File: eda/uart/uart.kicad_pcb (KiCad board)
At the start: 2 copper layers, 20 parts, among them J1 Bus expansion, U1 74HCT193, U2 74HCT165, U3 74HCT165, X1 1.8xx

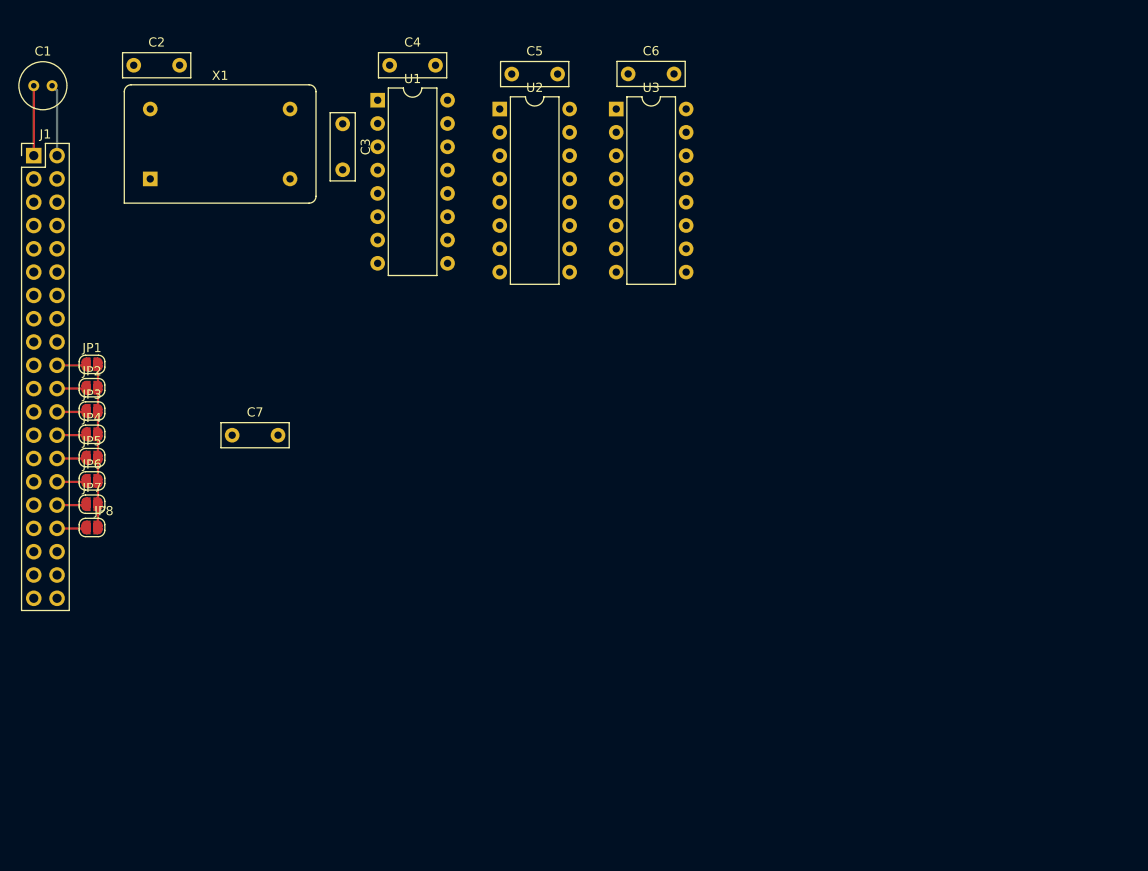
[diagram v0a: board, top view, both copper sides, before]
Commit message: More work on UART
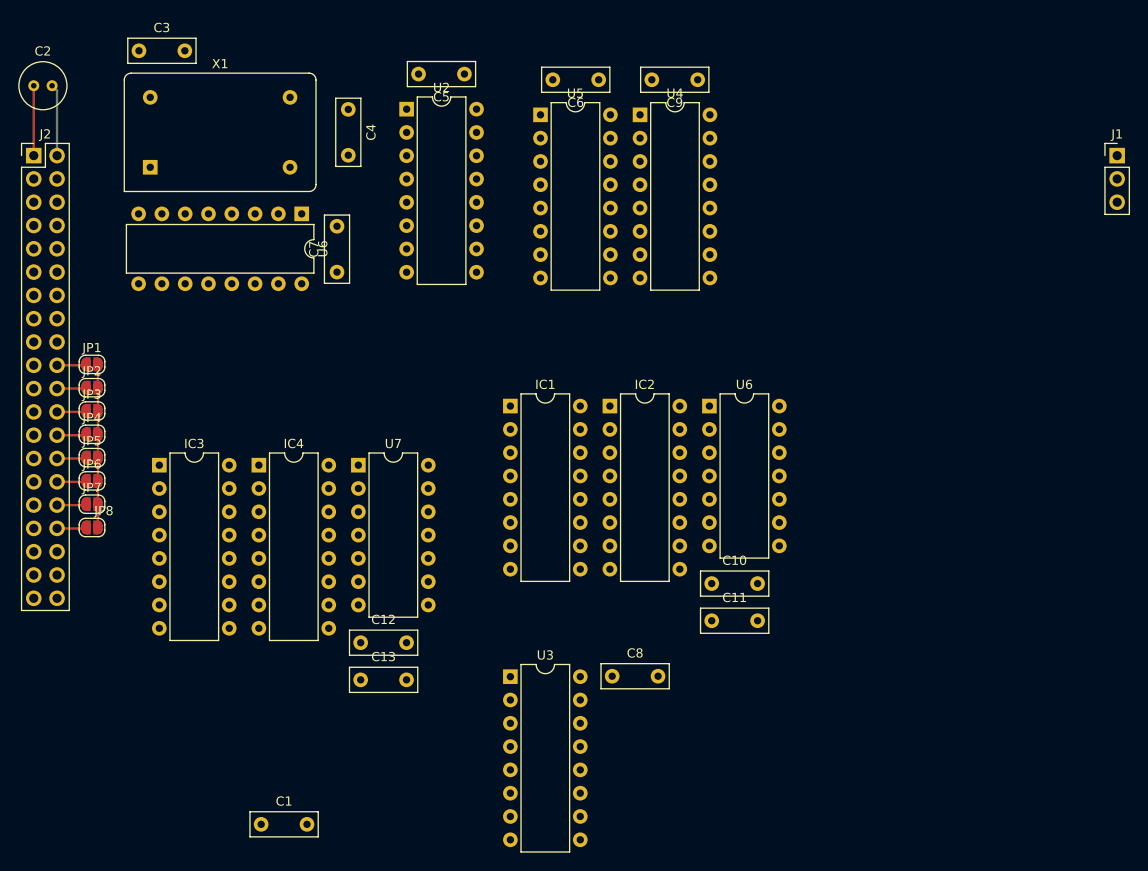
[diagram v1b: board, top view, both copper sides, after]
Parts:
- removed the C2 at (41.4, 81.6)
- removed U1: 74HCT193, Package_DIP:DIP-16_W7.62mm
- added C1: 0.1uf, Capacitor_THT:C_Rect_L7.2mm_W2.5mm_P5.00mm_FKS2_FKP2_MKS2_MKP2, F.Cu at (55.3, 164.3)
- added C10: 0.1uf, Capacitor_THT:C_Rect_L7.2mm_W2.5mm_P5.00mm_FKS2_FKP2_MKS2_MKP2, F.Cu at (104.4, 138.1)
- added C11: 0.1uf, Capacitor_THT:C_Rect_L7.2mm_W2.5mm_P5.00mm_FKS2_FKP2_MKS2_MKP2, F.Cu at (104.4, 142.1)
- added C12: 0.1uf, Capacitor_THT:C_Rect_L7.2mm_W2.5mm_P5.00mm_FKS2_FKP2_MKS2_MKP2, F.Cu at (66.1, 144.5)
- added C13: 0.1uf, Capacitor_THT:C_Rect_L7.2mm_W2.5mm_P5.00mm_FKS2_FKP2_MKS2_MKP2, F.Cu at (66.1, 148.6)
- added C8: 0.1uf, Capacitor_THT:C_Rect_L7.2mm_W2.5mm_P5.00mm_FKS2_FKP2_MKS2_MKP2, F.Cu at (93.5, 148.2)
- added C9: 0.1uf, Capacitor_THT:C_Rect_L7.2mm_W2.5mm_P5.00mm_FKS2_FKP2_MKS2_MKP2, F.Cu at (102.9, 83.2)
- added IC1: CD74HCT40105E, Package_DIP:DIP-16_W7.62mm, F.Cu at (82.4, 118.7)
- added IC2: CD74HCT40105E, Package_DIP:DIP-16_W7.62mm, F.Cu at (93.3, 118.7)
- added IC3: CD74HCT40105E, Package_DIP:DIP-16_W7.62mm, F.Cu at (44.2, 125.2)
- added IC4: CD74HCT40105E, Package_DIP:DIP-16_W7.62mm, F.Cu at (55.0, 125.2)
- added J1: UART, Connector_PinHeader_2.54mm:PinHeader_1x03_P2.54mm_Vertical, F.Cu at (148.6, 91.4)
- added U4: 74HCT165, Package_DIP:DIP-16_W7.62mm, F.Cu at (96.6, 87.0)
- added U5: 74HCT165, Package_DIP:DIP-16_W7.62mm, F.Cu at (85.7, 87.0)
- added U6: 74LS08, Package_DIP:DIP-14_W7.62mm, F.Cu at (104.1, 118.7)
- added U6: 74HCT139, Package_DIP:DIP-16_W7.62mm, F.Cu at (59.7, 97.8)
- added U7: 74HCT08, Package_DIP:DIP-14_W7.62mm, F.Cu at (65.9, 125.2)
- C4: value 0.1uf -> 22pf
- U2, U3: value 74HCT165 -> 74HCT193
- moved U3 63.0 mm to (82.4, 148.2)
- moved C3 23.6 mm to (42.0, 80.0), turned to 0 degrees
- moved C7 21.1 mm to (63.5, 104.1), turned to 90 degrees
- moved U2 10.2 mm to (71.1, 86.4)
- moved C4 6.59 mm to (64.8, 86.4), turned to -90 degrees
- moved C5 5.16 mm to (77.4, 82.5), turned to 180 degrees
- moved C6 3.28 mm to (92.1, 83.2), turned to 180 degrees
- moved X1 1.27 mm to (43.2, 92.7)
- renumbered C1 to C2, J1 to J2
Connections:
- net /Expansion header/CS renamed /Expansion header/~{CS}
- C3 pad 1: Net-(U1-UP) -> VCC
- C3 pad 2: GND -> Net-(U2-UP)
- C4 pad 1: VCC -> Net-(U2-UP)
- U2 pad 1: unconnected-(U2-~{PL}-Pad1) -> GND
- U2 pad 10: VCC -> GND
- U2 pad 11: unconnected-(U2-D0-Pad11) -> VCC
- U2 pad 13: unconnected-(U2-D2-Pad13) -> /clock/UartClock
- U2 pad 14: unconnected-(U2-D3-Pad14) -> GND
- U2 pad 15: unconnected-(U2-~{CE}-Pad15) -> GND
- U2 pad 5: unconnected-(U2-D6-Pad5) -> Net-(U2-UP)
- U2 pad 9: Net-(U2-Q7) -> GND
- U3 pad 10: Net-(U2-Q7) -> unconnected-(U3-C-Pad10)
- U3 pad 9: TX -> unconnected-(U3-D-Pad9)
- X1 pad 8: Net-(U1-UP) -> Net-(U2-UP)

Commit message: Port main board schematic to kicad
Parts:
- added C15: 0.1uf, Capacitor_THT:C_Rect_L7.2mm_W3.5mm_P5.00mm_FKS2_FKP2_MKS2_MKP2, F.Cu at (177.2, 21.6)
- added C16: 0.1uf, Capacitor_THT:C_Rect_L7.2mm_W3.5mm_P5.00mm_FKS2_FKP2_MKS2_MKP2, F.Cu at (90.9, 145.4)
- added C17: 0.1uf, Capacitor_THT:C_Rect_L7.2mm_W3.5mm_P5.00mm_FKS2_FKP2_MKS2_MKP2, F.Cu at (90.9, 150.5)
- added C2: 0.1uf, Capacitor_THT:C_Rect_L7.2mm_W3.5mm_P5.00mm_FKS2_FKP2_MKS2_MKP2, F.Cu at (268.2, 21.1)
- added U1: 74HCT08, Package_DIP:DIP-14_W7.62mm, F.Cu at (246.4, 29.8)
- added U10: 74HCT574, Package_DIP:DIP-20_W7.62mm, F.Cu at (175.9, 25.4)
- added U11: 74HCT595, Package_DIP:DIP-16_W7.62mm, F.Cu at (78.7, 135.3)
- added U12: 74HCT595, Package_DIP:DIP-16_W7.62mm, F.Cu at (58.4, 127.0)
- added U2: 74HCT14, Package_DIP:DIP-14_W7.62mm, F.Cu at (262.9, 34.3)
- C1: footprint Capacitor_THT:C_Rect_L7.2mm_W2.5mm_P5.00mm_FKS2_FKP2_MKS2_MKP2 -> Capacitor_THT:C_Rect_L7.2mm_W3.5mm_P5.00mm_FKS2_FKP2_MKS2_MKP2
- C10: renamed from C9; footprint Capacitor_THT:C_Rect_L7.2mm_W2.5mm_P5.00mm_FKS2_FKP2_MKS2_MKP2 -> Capacitor_THT:C_Rect_L7.2mm_W3.5mm_P5.00mm_FKS2_FKP2_MKS2_MKP2
- C11: renamed from C10; footprint Capacitor_THT:C_Rect_L7.2mm_W2.5mm_P5.00mm_FKS2_FKP2_MKS2_MKP2 -> Capacitor_THT:C_Rect_L7.2mm_W3.5mm_P5.00mm_FKS2_FKP2_MKS2_MKP2
- C12: renamed from C11; footprint Capacitor_THT:C_Rect_L7.2mm_W2.5mm_P5.00mm_FKS2_FKP2_MKS2_MKP2 -> Capacitor_THT:C_Rect_L7.2mm_W3.5mm_P5.00mm_FKS2_FKP2_MKS2_MKP2
- C13: renamed from C12; footprint Capacitor_THT:C_Rect_L7.2mm_W2.5mm_P5.00mm_FKS2_FKP2_MKS2_MKP2 -> Capacitor_THT:C_Rect_L7.2mm_W3.5mm_P5.00mm_FKS2_FKP2_MKS2_MKP2
- C14: renamed from C13; footprint Capacitor_THT:C_Rect_L7.2mm_W2.5mm_P5.00mm_FKS2_FKP2_MKS2_MKP2 -> Capacitor_THT:C_Rect_L7.2mm_W3.5mm_P5.00mm_FKS2_FKP2_MKS2_MKP2
- C4: renamed from C3; footprint Capacitor_THT:C_Rect_L7.2mm_W2.5mm_P5.00mm_FKS2_FKP2_MKS2_MKP2 -> Capacitor_THT:C_Rect_L7.2mm_W3.5mm_P5.00mm_FKS2_FKP2_MKS2_MKP2
- C5: renamed from C4; footprint Capacitor_THT:C_Rect_L7.2mm_W2.5mm_P5.00mm_FKS2_FKP2_MKS2_MKP2 -> Capacitor_THT:C_Rect_L7.2mm_W3.5mm_P5.00mm_FKS2_FKP2_MKS2_MKP2
- C6: renamed from C5; footprint Capacitor_THT:C_Rect_L7.2mm_W2.5mm_P5.00mm_FKS2_FKP2_MKS2_MKP2 -> Capacitor_THT:C_Rect_L7.2mm_W3.5mm_P5.00mm_FKS2_FKP2_MKS2_MKP2
- C7: renamed from C6; footprint Capacitor_THT:C_Rect_L7.2mm_W2.5mm_P5.00mm_FKS2_FKP2_MKS2_MKP2 -> Capacitor_THT:C_Rect_L7.2mm_W3.5mm_P5.00mm_FKS2_FKP2_MKS2_MKP2
- C8: renamed from C7; footprint Capacitor_THT:C_Rect_L7.2mm_W2.5mm_P5.00mm_FKS2_FKP2_MKS2_MKP2 -> Capacitor_THT:C_Rect_L7.2mm_W3.5mm_P5.00mm_FKS2_FKP2_MKS2_MKP2
- C9: renamed from C8; footprint Capacitor_THT:C_Rect_L7.2mm_W2.5mm_P5.00mm_FKS2_FKP2_MKS2_MKP2 -> Capacitor_THT:C_Rect_L7.2mm_W3.5mm_P5.00mm_FKS2_FKP2_MKS2_MKP2
- JP1, JP2, JP3, JP4, JP5, JP6, JP7, JP8: moved to B.Cu
- moved C1 255.2 mm to (275.6, 35.6)
- moved C9 182.9 mm to (234.0, 31.1)
- moved U4 182.9 mm to (222.9, 31.1)
- moved U7 157.5 mm to (191.1, 29.6)
- moved U6 134.0 mm to (205.2, 30.8)
- moved C11 82.1 mm to (38.7, 88.9), turned to 90 degrees
- moved C12 73.2 mm to (38.7, 109.8), turned to 90 degrees
- moved C13 62.0 mm to (78.7, 83.8), turned to -90 degrees
- moved U8 52.5 mm to (43.2, 83.8)
- moved U9 52.0 mm to (43.2, 104.8)
- moved IC1 47.1 mm to (66.7, 83.8)
- moved C10 43.4 mm to (62.2, 67.9)
- moved X1 42.3 mm to (80.6, 112.4)
- moved C4 42.3 mm to (79.4, 99.7)
- moved C5 42.3 mm to (102.2, 106.1)
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- renumbered C2 to C3, IC3 to IC1, IC4 to IC2, U2 to U3, U3 to U4, U4 to U5, U5 to U6, U6 to U7, IC1 to U8, IC2 to U9
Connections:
- IC1 pad 14: Net-(IC3-DOR) -> Net-(IC1-DOR)
- IC1 pad 2: Net-(IC3-DIR) -> Net-(IC1-DIR)
- IC1 pad 9: /recieve/FIFO/Reset -> /recieve/Reset
- IC2 pad 14: Net-(IC4-DOR) -> Net-(IC2-DOR)
- IC2 pad 2: Net-(IC4-DIR) -> Net-(IC2-DIR)
- IC2 pad 9: /recieve/FIFO/Reset -> /recieve/Reset
- U4 pad 1: unconnected-(U3-B-Pad1) -> GND
- U4 pad 10: unconnected-(U3-C-Pad10) -> VCC
- U4 pad 11: unconnected-(U3-~{LOAD}-Pad11) -> /transmit/FIFO/DOR
- U4 pad 13: unconnected-(U3-~{BO}-Pad13) -> /transmit/FIFO/SO
- U4 pad 14: unconnected-(U3-CLR-Pad14) -> GND
- U4 pad 15: unconnected-(U3-A-Pad15) -> GND
- U4 pad 4: unconnected-(U3-DOWN-Pad4) (its old number) -> /clock/UartClock
- U4 pad 9: unconnected-(U3-D-Pad9) -> VCC
- U5 pad 1: unconnected-(U4-~{PL}-Pad1) -> ~{LatchShiftRegisters}
- U5 pad 11: unconnected-(U4-D0-Pad11) -> /transmit/FIFO/Q6
- U5 pad 12: unconnected-(U4-D1-Pad12) -> /transmit/FIFO/Q5
- U5 pad 13: unconnected-(U4-D2-Pad13) -> /transmit/FIFO/Q4
- U5 pad 14: unconnected-(U4-D3-Pad14) -> /transmit/FIFO/Q3
- U5 pad 15: unconnected-(U4-~{CE}-Pad15) -> GND
- U5 pad 2: unconnected-(U4-CP-Pad2) -> /clock/UartClock
- U5 pad 3: unconnected-(U4-D4-Pad3) -> /transmit/FIFO/Q2
- U5 pad 4: unconnected-(U4-D5-Pad4) -> /transmit/FIFO/Q1
- U5 pad 5: unconnected-(U4-D6-Pad5) -> /transmit/FIFO/Q0
- U5 pad 6: unconnected-(U4-D7-Pad6) -> GND
- U6 pad 1: unconnected-(U5-~{PL}-Pad1) -> ~{LatchShiftRegisters}
- U6 pad 11: unconnected-(U5-D0-Pad11) -> VCC
- U6 pad 12: unconnected-(U5-D1-Pad12) -> VCC
- U6 pad 13: unconnected-(U5-D2-Pad13) -> VCC
- U6 pad 14: unconnected-(U5-D3-Pad14) -> VCC
- U6 pad 15: unconnected-(U5-~{CE}-Pad15) -> GND
- U6 pad 2: unconnected-(U5-CP-Pad2) -> /clock/UartClock
- U6 pad 3: unconnected-(U5-D4-Pad3) -> VCC
- U6 pad 4: unconnected-(U5-D5-Pad4) -> VCC
- U6 pad 5: unconnected-(U5-D6-Pad5) -> VCC
- U6 pad 6: unconnected-(U5-D7-Pad6) -> /transmit/FIFO/Q7
- U8 pad 14: Net-(IC1-DOR) -> Net-(U8-DOR)
- U8 pad 2: Net-(IC1-DIR) -> Net-(U8-DIR)
- U8 pad 3: /transmit/FIFO/SI -> /address_decode/~{TransmitEnable}
- U8 pad 9: /transmit/FIFO/Reset -> /recieve/Reset
- U9 pad 14: Net-(IC2-DOR) -> Net-(U9-DOR)
- U9 pad 2: Net-(IC2-DIR) -> Net-(U9-DIR)
- U9 pad 3: /transmit/FIFO/SI -> /address_decode/~{TransmitEnable}
- U9 pad 9: /transmit/FIFO/Reset -> /recieve/Reset
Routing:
- net VCC: track 7.62 -> 142.0 mm
- net GND: track 7.84 -> 125.9 mm
- net /transmit/FIFO/Q7: track 0.00 -> 74.7 mm
- net /Expansion header/D7: track 0.00 -> 48.7 mm
- net /Expansion header/D6: track 0.00 -> 48.0 mm
- net /Expansion header/D4: track 0.00 -> 47.4 mm
- net /transmit/FIFO/Q6: track 0.00 -> 47.4 mm
- net /Expansion header/D5: track 0.00 -> 47.2 mm
- net /transmit/FIFO/Q4: track 0.00 -> 47.1 mm
- net /Expansion header/D1: track 0.00 -> 45.1 mm
- net /Expansion header/D2: track 0.00 -> 45.1 mm
- net /Expansion header/D3: track 0.00 -> 45.1 mm
- net /transmit/FIFO/Q5: track 0.00 -> 44.3 mm
- net /Expansion header/D0: track 0.00 -> 43.3 mm
- net /transmit/FIFO/Q3: track 0.00 -> 38.6 mm
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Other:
- board outline added: 122.6 x 85.1 mm

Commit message: Work on main board eda, interim
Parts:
- removed the U6 at (205.2, 30.8)
- removed the U7 at (191.1, 29.6)
- moved C2 241.4 mm to (60.0, 143.3)
- moved U2 230.9 mm to (56.4, 137.7), turned to -90 degrees
- moved C1 199.9 mm to (90.4, 111.0), turned to -90 degrees
- moved U1 174.8 mm to (95.5, 118.1), turned to 90 degrees
- moved C9 132.1 mm to (107.2, 68.1), turned to 180 degrees
- moved U10 116.9 mm to (77.7, 88.9)
- moved U4 110.7 mm to (119.9, 71.6), turned to -90 degrees
- moved C15 110.0 mm to (86.4, 83.8)
- moved C6 30.4 mm to (114.5, 84.6), turned to 180 degrees
- moved C16 26.9 mm to (65.0, 138.2), turned to 180 degrees
- moved C5 23.2 mm to (95.5, 83.8), turned to 0 degrees
- moved X1 22.8 mm to (102.1, 104.6), turned to 90 degrees
- moved U3 21.1 mm to (108.2, 88.4), turned to 0 degrees
- moved J1 15.9 mm to (126.5, 78.7)
- moved C17 15.3 mm to (81.8, 138.2), turned to 180 degrees
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- renumbered IC1 to U13, IC2 to U14
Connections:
- net /recieve/FIFO/SI renamed /recieve/FIFO Recieve/SI
- net /recieve/FIFO/SO renamed /recieve/FIFO Recieve/SO
- net /transmit/FIFO/DOR renamed /transmit/FIFO Transmit/DOR
- net /transmit/FIFO/Q0 renamed /transmit/FIFO Transmit/Q0
- net /transmit/FIFO/Q1 renamed /transmit/FIFO Transmit/Q1
- net /transmit/FIFO/Q2 renamed /transmit/FIFO Transmit/Q2
- net /transmit/FIFO/Q3 renamed /transmit/FIFO Transmit/Q3
- net /transmit/FIFO/Q4 renamed /transmit/FIFO Transmit/Q4
- net /transmit/FIFO/Q5 renamed /transmit/FIFO Transmit/Q5
- net /transmit/FIFO/Q6 renamed /transmit/FIFO Transmit/Q6
- net /transmit/FIFO/Q7 renamed /transmit/FIFO Transmit/Q7
- net /transmit/FIFO/SO renamed /transmit/FIFO Transmit/SO
- U1 pad 11: /recieve/FIFO/DOR -> /recieve/FIFO Recieve/DOR
- U11 pad 14: /Expansion header/D6 -> /recieve/FIFO Recieve/D6
- U11 pad 15: /Expansion header/D7 -> /recieve/FIFO Recieve/D7
- U12 pad 1: /Expansion header/D0 -> /recieve/FIFO Recieve/D0
- U12 pad 2: /Expansion header/D1 -> /recieve/FIFO Recieve/D1
- U12 pad 3: /Expansion header/D2 -> /recieve/FIFO Recieve/D2
- U12 pad 4: /Expansion header/D3 -> /recieve/FIFO Recieve/D3
- U12 pad 5: /Expansion header/D4 -> /recieve/FIFO Recieve/D4
- U12 pad 6: /Expansion header/D5 -> /recieve/FIFO Recieve/D5
- U12 pad 7: /Expansion header/D6 -> /recieve/FIFO Recieve/D6
- U13 pad 10: /Expansion header/D3 -> /recieve/DOut3
- U13 pad 11: /Expansion header/D2 -> /recieve/DOut2
- U13 pad 12: /Expansion header/D1 -> /recieve/DOut1
- U13 pad 13: /Expansion header/D0 -> /recieve/DOut0
- U13 pad 4: /recieve/FIFO/D0 -> /recieve/FIFO Recieve/D0
- U13 pad 5: /recieve/FIFO/D1 -> /recieve/FIFO Recieve/D1
- U13 pad 6: /recieve/FIFO/D2 -> /recieve/FIFO Recieve/D2
- U13 pad 7: /recieve/FIFO/D3 -> /recieve/FIFO Recieve/D3
- U14 pad 10: /Expansion header/D7 -> /recieve/DOut7
- U14 pad 11: /Expansion header/D6 -> /recieve/DOut6
- U14 pad 12: /Expansion header/D5 -> /recieve/DOut5
- U14 pad 13: /Expansion header/D4 -> /recieve/DOut4
- U14 pad 4: /recieve/FIFO/D4 -> /recieve/FIFO Recieve/D4
- U14 pad 5: /recieve/FIFO/D5 -> /recieve/FIFO Recieve/D5
- U14 pad 6: /recieve/FIFO/D6 -> /recieve/FIFO Recieve/D6
- U14 pad 7: /recieve/FIFO/D7 -> /recieve/FIFO Recieve/D7
- U2 pad 1: /Expansion header/~{RST} -> (no net)
- U2 pad 2: /recieve/Reset -> (no net)
- U2 pad 5: (no net) -> /Expansion header/~{RST}
- U2 pad 6: (no net) -> /recieve/Reset
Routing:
- net GND: track 125.9 -> 289.4 mm
- net VCC: track 142.0 -> 237.0 mm
- net /Expansion header/Clock: track 0.00 -> 86.7 mm
- net /recieve/Reset: track 0.00 -> 69.4 mm
- net /recieve/FIFO Recieve/D6: track 0.00 -> 53.9 mm, vias 0 -> 1
- net /recieve/FIFO Recieve/D3: track 0.00 -> 45.7 mm
- net /recieve/FIFO Recieve/D2: track 0.00 -> 42.8 mm
- net /recieve/FIFO Recieve/D1: track 0.00 -> 42.0 mm
- net /recieve/FIFO Recieve/D0: track 0.00 -> 39.0 mm
- net /recieve/FIFO Recieve/D5: track 0.00 -> 38.7 mm
- net /recieve/FIFO Recieve/D4: track 0.00 -> 34.6 mm
- net /recieve/FIFO Recieve/D7: track 0.00 -> 22.7 mm
- net /Expansion header/D7: track 48.7 -> 69.8 mm
- net /Expansion header/D6: track 48.0 -> 68.6 mm
- net /Expansion header/D5: track 47.2 -> 67.8 mm
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
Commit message: Update eda
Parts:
- added C18: 0.1uf, Capacitor_THT:C_Rect_L7.2mm_W3.5mm_P5.00mm_FKS2_FKP2_MKS2_MKP2, F.Cu at (199.3, 59.4)
- added C19: 0.1uf, Capacitor_THT:C_Rect_L7.2mm_W3.5mm_P5.00mm_FKS2_FKP2_MKS2_MKP2, F.Cu at (37.6, 114.5)
- added U16: 74HCT14, Package_DIP:DIP-14_W7.62mm, F.Cu at (201.1, 70.1)
- added U17: 74HCT193, Package_DIP:DIP-16_W7.62mm, F.Cu at (213.9, 70.1)
- added U18: 74HCT32, Package_DIP:DIP-14_W7.62mm, F.Cu at (43.9, 110.2)
- added U7: 74HCT139, Package_DIP:DIP-16_W7.62mm, F.Cu at (44.2, 137.4)
- moved C1 127.9 mm to (156.5, 1.52)
- moved C13 127.9 mm to (143.8, -25.7)
- moved C14 127.9 mm to (145.3, 8.89)
- moved C9 127.9 mm to (173.2, -41.4)
- moved U10 127.9 mm to (143.8, -20.6)
- moved U13 127.9 mm to (132.7, -25.7)
- moved U14 127.9 mm to (132.7, -4.70)
- moved U7 127.9 mm to (95.9, -30.1)
- moved C15 127.9 mm to (152.4, -25.7)
- moved C16 127.9 mm to (131.1, 28.7)
- moved C17 127.9 mm to (147.8, 28.7)
- moved C2 127.9 mm to (126.0, 33.8)
- moved C4 127.9 mm to (155.2, -3.60)
- moved C5 127.9 mm to (161.6, -25.7)
- moved C6 127.9 mm to (180.5, -24.9)
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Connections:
- net ~{LatchShiftRegisters} renamed /transmit/~{LatchShiftRegisters}
- U1 pad 11: /recieve/FIFO Recieve/DOR -> /recieve/DataAvailable
- U10 pad 4: unconnected-(U10-D2-Pad4) -> /recieve/DataAvailable
- U10 pad 5: unconnected-(U10-D3-Pad5) -> GND
- U10 pad 6: unconnected-(U10-D4-Pad6) -> GND
- U10 pad 7: unconnected-(U10-D5-Pad7) -> GND
- U10 pad 8: unconnected-(U10-D6-Pad8) -> GND
- U10 pad 9: unconnected-(U10-D7-Pad9) -> GND
- U11 pad 10: VCC -> Net-(U11-~{SRCLR})
- U11 pad 11: unconnected-(U11-SRCLK-Pad11) -> /clock/UartClock
- U11 pad 12: unconnected-(U11-RCLK-Pad12) -> /clock/UartClock
- U12 pad 10: VCC -> Net-(U11-~{SRCLR})
- U12 pad 11: unconnected-(U12-SRCLK-Pad11) -> /clock/UartClock
- U12 pad 12: unconnected-(U12-RCLK-Pad12) -> /clock/UartClock
- U13 pad 10: /recieve/DOut3 -> /Expansion header/D3
- U13 pad 11: /recieve/DOut2 -> /Expansion header/D2
- U13 pad 12: /recieve/DOut1 -> /Expansion header/D1
- U13 pad 13: /recieve/DOut0 -> /Expansion header/D0
- U13 pad 3: /recieve/FIFO Recieve/SI -> /recieve/Reset
- U14 pad 10: /recieve/DOut7 -> /Expansion header/D7
- U14 pad 11: /recieve/DOut6 -> /Expansion header/D6
- U14 pad 12: /recieve/DOut5 -> /Expansion header/D5
- U14 pad 13: /recieve/DOut4 -> /Expansion header/D4
- U14 pad 3: /recieve/FIFO Recieve/SI -> /recieve/Reset
- U2 pad 1: (no net) -> /Expansion header/~{CS}
- U2 pad 10: (no net) -> /address_decode/TransmitEnable
- U2 pad 11: (no net) -> Net-(U7A-O0)
- U2 pad 2: (no net) -> Net-(U15-Pad1)
- U2 pad 8: (no net) -> Net-(U18-Pad2)
- U2 pad 9: (no net) -> /Expansion header/R~{W}
- U4 pad 2: unconnected-(U4-QB-Pad2) -> Net-(U4-QB)
- U4 pad 3: unconnected-(U4-QA-Pad3) -> Net-(U4-QA)
- U4 pad 5: unconnected-(U4-UP-Pad5) -> VCC
- U4 pad 7: unconnected-(U4-QD-Pad7) -> Net-(U4-QD)
- U5 pad 11: /transmit/FIFO Transmit/Q6 -> /transmit/FIFO Transmit/Q5
- U5 pad 12: /transmit/FIFO Transmit/Q5 -> /transmit/FIFO Transmit/Q4
- U5 pad 13: /transmit/FIFO Transmit/Q4 -> /transmit/FIFO Transmit/Q3
- U5 pad 14: /transmit/FIFO Transmit/Q3 -> /transmit/FIFO Transmit/Q2
- U5 pad 3: /transmit/FIFO Transmit/Q2 -> /transmit/FIFO Transmit/Q1
- U5 pad 4: /transmit/FIFO Transmit/Q1 -> /transmit/FIFO Transmit/Q0
- U5 pad 5: /transmit/FIFO Transmit/Q0 -> GND
- U5 pad 6: GND -> VCC
- U6 pad 5: VCC -> /transmit/FIFO Transmit/Q7
- U6 pad 6: /transmit/FIFO Transmit/Q7 -> /transmit/FIFO Transmit/Q6
- U8 pad 3: /address_decode/~{TransmitEnable} -> /address_decode/TransmitEnable
- U9 pad 3: /address_decode/~{TransmitEnable} -> /address_decode/TransmitEnable
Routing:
- net GND: track 289.4 -> 0.00 mm
- net VCC: track 237.0 -> 0.00 mm
- net /Expansion header/Clock: track 86.7 -> 0.00 mm
- net /transmit/FIFO Transmit/Q7: track 74.7 -> 0.00 mm
- net /Expansion header/D7: track 69.8 -> 0.00 mm
- net /recieve/Reset: track 69.4 -> 0.00 mm
- net /Expansion header/D6: track 68.6 -> 0.00 mm
- net /Expansion header/D5: track 67.8 -> 0.00 mm
- net /Expansion header/D4: track 66.8 -> 0.00 mm
- net /Expansion header/D3: track 59.2 -> 0.00 mm
- net /Expansion header/D1: track 58.8 -> 0.00 mm
- net /Expansion header/D2: track 58.2 -> 0.00 mm
- net /Expansion header/D0: track 56.4 -> 0.00 mm
- net /recieve/FIFO Recieve/D6: track 53.9 -> 0.00 mm, vias 1 -> 0
- net /transmit/FIFO Transmit/Q6: track 47.4 -> 0.00 mm
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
